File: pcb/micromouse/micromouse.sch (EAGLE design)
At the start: 66 parts, among them IC1 LM2575-5.0WU-(TR), IC2 LM2575-3.3WU-(TR), IC3 DSPIC33FJ64MC804-PT, IC4 L293D, Y1 7.3728MHz

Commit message: Change comment next to series resistors of LEDs (voltage was wrong)
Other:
- note added: "10mA @ 1.2 V"
- note removed: "10mA @ 1.21 V"
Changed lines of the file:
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@@
 max. output current of uC = 15mA.</text>
 <text x="264.16" y="251.46" size="1.778" layer="91">10mA @ 2.1 V</text>
-<text x="264.16" y="261.62" size="1.778" layer="91">10mA @ 1.21 V</text>
+<text x="264.16" y="261.62" size="1.778" layer="91">10mA @ 1.2 V</text>
 <text x="304.8" y="154.94" size="1.778" layer="91">Use socket instead of soldering the
 chip directly onto the board.</text>

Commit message: Fixed ground plate isolation distance, mounting holes and errors
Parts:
- PAD1: value (none) -> TEST_GND
- PAD10: value (none) -> TEST_AVDD
- PAD11: value (none) -> TEST_AVSS
- PAD2: value (none) -> TEST_9V
- PAD3: value (none) -> TEST_5V
- PAD4: value (none) -> TEST_3V3
- PAD5: value (none) -> TEST_PWM1L2
- PAD6: value (none) -> TEST_PWM1L1
- PAD7: value (none) -> TEST_IR0
- PAD8: value (none) -> TEST_IR1
- PAD9: value (none) -> TEST_IR2
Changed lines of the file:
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@@
 <part name="L1" library="Eagle_WE-TIS (rev22a)" deviceset="WE-TIS_1111" device="" package3d_urn="urn:adsk.eagle:package:12988462/4" technology="_7447471331" value="330uH"/>
 <part name="L2" library="Eagle_WE-TIS (rev22a)" deviceset="WE-TIS_1111" device="" package3d_urn="urn:adsk.eagle:package:12988462/4" technology="_7447471331" value="330uH"/>
-<part name="PAD2" library="wirepad" library_urn="urn:adsk.eagle:library:412" deviceset="3,17/1,3" device="" package3d_urn="urn:adsk.eagle:package:30833/1"/>
-<part name="PAD3" library="wirepad" library_urn="urn:adsk.eagle:library:412" deviceset="3,17/1,3" device="" package3d_urn="urn:adsk.eagle:package:30833/1"/>
-<part name="PAD4" library="wirepad" library_urn="urn:adsk.eagle:library:412" deviceset="3,17/1,3" device="" package3d_urn="urn:adsk.eagle:package:30833/1"/>
-<part name="PAD7" library="wirepad" library_urn="urn:adsk.eagle:library:412" deviceset="3,17/1,3" device="" package3d_urn="urn:adsk.eagle:package:30833/1"/>
-<part name="PAD8" library="wirepad" library_urn="urn:adsk.eagle:library:412" deviceset="3,17/1,3" device="" package3d_urn="urn:adsk.eagle:package:30833/1"/>
-<part name="PAD9" library="wirepad" library_urn="urn:adsk.eagle:library:412" deviceset="3,17/1,3" device="" package3d_urn="urn:adsk.eagle:package:30833/1"/>
-<part name="PAD10" library="wirepad" library_urn="urn:adsk.eagle:library:412" deviceset="3,17/1,3" device="" package3d_urn="urn:adsk.eagle:package:30833/1"/>
-<part name="PAD5" library="wirepad" library_urn="urn:adsk.eagle:library:412" deviceset="3,17/1,3" device="" package3d_urn="urn:adsk.eagle:package:30833/1"/>
-<part name="PAD6" library="wirepad" library_urn="urn:adsk.eagle:library:412" deviceset="3,17/1,3" device="" package3d_urn="urn:adsk.eagle:package:30833/1"/>
-<part name="PAD1" library="wirepad" library_urn="urn:adsk.eagle:library:412" deviceset="3,17/1,3" device="" package3d_urn="urn:adsk.eagle:package:30833/1"/>
-<part name="PAD11" library="wirepad" library_urn="urn:adsk.eagle:library:412" deviceset="3,17/1,3" device="" package3d_urn="urn:adsk.eagle:package:30833/1"/>
+<part name="PAD2" library="wirepad" library_urn="urn:adsk.eagle:library:412" deviceset="3,17/1,3" device="" package3d_urn="urn:adsk.eagle:package:30833/1" value="TEST_9V"/>
+<part name="PAD3" library="wirepad" library_urn="urn:adsk.eagle:library:412" deviceset="3,17/1,3" device="" package3d_urn="urn:adsk.eagle:package:30833/1" value="TEST_5V"/>
+<part name="PAD4" library="wirepad" library_urn="urn:adsk.eagle:library:412" deviceset="3,17/1,3" device="" package3d_urn="urn:adsk.eagle:package:30833/1" value="TEST_3V3"/>
+<part name="PAD7" library="wirepad" library_urn="urn:adsk.eagle:library:412" deviceset="3,17/1,3" device="" package3d_urn="urn:adsk.eagle:package:30833/1" value="TEST_IR0"/>
+<part name="PAD8" library="wirepad" library_urn="urn:adsk.eagle:library:412" deviceset="3,17/1,3" device="" package3d_urn="urn:adsk.eagle:package:30833/1" value="TEST_IR1"/>
+<part name="PAD9" library="wirepad" library_urn="urn:adsk.eagle:library:412" deviceset="3,17/1,3" device="" package3d_urn="urn:adsk.eagle:package:30833/1" value="TEST_IR2"/>
+<part name="PAD10" library="wirepad" library_urn="urn:adsk.eagle:library:412" deviceset="3,17/1,3" device="" package3d_urn="urn:adsk.eagle:package:30833/1" value="TEST_AVDD"/>
+<part name="PAD5" library="wirepad" library_urn="urn:adsk.eagle:library:412" deviceset="3,17/1,3" device="" package3d_urn="urn:adsk.eagle:package:30833/1" value="TEST_PWM1L2"/>
+<part name="PAD6" library="wirepad" library_urn="urn:adsk.eagle:library:412" deviceset="3,17/1,3" device="" package3d_urn="urn:adsk.eagle:package:30833/1" value="TEST_PWM1L1"/>
+<part name="PAD1" library="wirepad" library_urn="urn:adsk.eagle:library:412" deviceset="3,17/1,3" device="" package3d_urn="urn:adsk.eagle:package:30833/1" value="TEST_GND"/>
+<part name="PAD11" library="wirepad" library_urn="urn:adsk.eagle:library:412" deviceset="3,17/1,3" device="" package3d_urn="urn:adsk.eagle:package:30833/1" value="TEST_AVSS"/>
 <part name="C5" library="Eagle_WCAP-ATG5 (rev21a)" deviceset="WCAP-ATG5_6.3X11" device="" package3d_urn="urn:adsk.eagle:package:18308010/2" technology="_860020273010" value="330  uF "/>
 <part name="C6" library="Eagle_WCAP-ATG5 (rev21a)" deviceset="WCAP-ATG5_6.3X11" device="" package3d_urn="urn:adsk.eagle:package:18308010/2" technology="_860020273010" value="330  uF "/>
@@
 <instance part="PAD2" gate="1" x="-73.66" y="342.9" smashed="yes" rot="R90">
 <attribute name="NAME" x="-72.9742" y="334.137" size="1.778" layer="95" rot="R90"/>
-<attribute name="VALUE" x="-70.358" y="341.757" size="1.778" layer="96" rot="R90"/>
+<attribute name="VALUE" x="-70.358" y="334.137" size="1.778" layer="96" rot="R90"/>
 </instance>
 <instance part="PAD3" gate="1" x="27.94" y="342.9" smashed="yes" rot="R180">
 <attribute name="NAME" x="36.703" y="343.5858" size="1.778" layer="95" rot="R180"/>
-<attribute name="VALUE" x="29.083" y="346.202" size="1.778" layer="96" rot="R180"/>
+<attribute name="VALUE" x="36.703" y="341.122" size="1.778" layer="96" rot="R180"/>
 </instance>
 <instance part="PAD4" gate="1" x="27.94" y="292.1" smashed="yes" rot="R180">
 <attribute name="NAME" x="36.703" y="292.7858" size="1.778" layer="95" rot="R180"/>
-<attribute name="VALUE" x="29.083" y="295.402" size="1.778" layer="96" rot="R180"/>
+<attribute name="VALUE" x="36.703" y="290.322" size="1.778" layer="96" rot="R180"/>
 </instance>
 <instance part="PAD7" gate="1" x="147.32" y="309.88" smashed="yes" rot="R180">
 <attribute name="NAME" x="156.083" y="310.5658" size="1.778" layer="95" rot="R180"/>
-<attribute name="VALUE" x="148.463" y="313.182" size="1.778" layer="96" rot="R180"/>
+<attribute name="VALUE" x="161.163" y="308.102" size="1.778" layer="96" rot="R180"/>
 </instance>
 <instance part="PAD8" gate="1" x="147.32" y="292.1" smashed="yes" rot="R180">
 <attribute name="NAME" x="156.083" y="292.7858" size="1.778" layer="95" rot="R180"/>
-<attribute name="VALUE" x="148.463" y="295.402" size="1.778" layer="96" rot="R180"/>
+<attribute name="VALUE" x="161.163" y="290.322" size="1.778" layer="96" rot="R180"/>
 </instance>
 <instance part="PAD9" gate="1" x="147.32" y="274.32" smashed="yes" rot="R180">
 <attribute name="NAME" x="156.083" y="275.0058" size="1.778" layer="95" rot="R180"/>
-<attribute name="VALUE" x="148.463" y="277.622" size="1.778" layer="96" rot="R180"/>
+<attribute name="VALUE" x="161.163" y="272.542" size="1.778" layer="96" rot="R180"/>
 </instance>
 <instance part="PAD10" gate="1" x="154.94" y="66.04" smashed="yes" rot="R180">
 <attribute name="NAME" x="166.243" y="66.7258" size="1.778" layer="95" rot="R180"/>
-<attribute name="VALUE" x="156.083" y="69.342" size="1.778" layer="96" rot="R180"/>
+<attribute name="VALUE" x="166.243" y="64.262" size="1.778" layer="96" rot="R180"/>
 </instance>
 <instance part="PAD5" gate="1" x="58.42" y="134.62" smashed="yes">
 <attribute name="NAME" x="49.657" y="133.9342" size="1.778" layer="95"/>
-<attribute name="VALUE" x="57.277" y="131.318" size="1.778" layer="96"/>
+<attribute name="VALUE" x="42.037" y="131.318" size="1.778" layer="96"/>
 </instance>
 <instance part="PAD6" gate="1" x="58.42" y="124.46" smashed="yes">
 <attribute name="NAME" x="49.657" y="123.7742" size="1.778" layer="95"/>
-<attribute name="VALUE" x="57.277" y="121.158" size="1.778" layer="96"/>
+<attribute name="VALUE" x="42.037" y="121.158" size="1.778" layer="96"/>
 </instance>
 <instance part="PAD1" gate="1" x="-86.36" y="340.36" smashed="yes" rot="R180">
 <attribute name="NAME" x="-77.597" y="341.0458" size="1.778" layer="95" rot="R180"/>
-<attribute name="VALUE" x="-85.217" y="343.662" size="1.778" layer="96" rot="R180"/>
+<attribute name="VALUE" x="-77.597" y="338.582" size="1.778" layer="96" rot="R180"/>
 </instance>
 <instance part="PAD11" gate="1" x="154.94" y="53.34" smashed="yes" rot="R180">
 <attribute name="NAME" x="166.243" y="54.0258" size="1.778" layer="95" rot="R180"/>
-<attribute name="VALUE" x="156.083" y="56.642" size="1.778" layer="96" rot="R180"/>
+<attribute name="VALUE" x="166.243" y="51.562" size="1.778" layer="96" rot="R180"/>
 </instance>
 <instance part="C5" gate="G$1" x="25.4" y="325.12" smashed="yes" rot="R90">

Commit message: Almost final steps of PCB, before moving the oscillator
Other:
- note added: "+"
- note added: "Tantulum"
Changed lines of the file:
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@@
 depending on switch position.</text>
 <text x="-58.42" y="223.52" size="1.778" layer="91">Remove some IO if unable to draw all PCB lines</text>
+<text x="8.89" y="115.062" size="1.778" layer="91">+</text>
+<text x="9.144" y="109.982" size="1.778" layer="91">Tantulum</text>
 </plain>
 <instances>

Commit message: Add group name, move via next to oscillator and replace LEDs with low current LEDs.
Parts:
- R5, R7, R9: value 120R -> 680R
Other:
- note added: "2mA * 680R = 1.36V"
- note added: "2mA, 1.9V"
- note removed: "10mA @ 1.2 V"
- note removed: "10mA @ 2.1 V"
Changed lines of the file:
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@@
 <part name="GND11" library="supply1" library_urn="urn:adsk.eagle:library:371" deviceset="GND" device=""/>
 <part name="R1" library="rcl" library_urn="urn:adsk.eagle:library:334" deviceset="R-EU_" device="R0805" package3d_urn="urn:adsk.eagle:package:23553/2" value="10kR"/>
-<part name="R5" library="rcl" library_urn="urn:adsk.eagle:library:334" deviceset="R-EU_" device="R0805" package3d_urn="urn:adsk.eagle:package:23553/2" value="120R"/>
-<part name="R7" library="rcl" library_urn="urn:adsk.eagle:library:334" deviceset="R-EU_" device="R0805" package3d_urn="urn:adsk.eagle:package:23553/2" value="120R"/>
-<part name="R9" library="rcl" library_urn="urn:adsk.eagle:library:334" deviceset="R-EU_" device="R0805" package3d_urn="urn:adsk.eagle:package:23553/2" value="120R"/>
+<part name="R5" library="rcl" library_urn="urn:adsk.eagle:library:334" deviceset="R-EU_" device="R0805" package3d_urn="urn:adsk.eagle:package:23553/2" value="680R"/>
+<part name="R7" library="rcl" library_urn="urn:adsk.eagle:library:334" deviceset="R-EU_" device="R0805" package3d_urn="urn:adsk.eagle:package:23553/2" value="680R"/>
+<part name="R9" library="rcl" library_urn="urn:adsk.eagle:library:334" deviceset="R-EU_" device="R0805" package3d_urn="urn:adsk.eagle:package:23553/2" value="680R"/>
 <part name="C14" library="rcl" library_urn="urn:adsk.eagle:library:334" deviceset="C-EU" device="C0805" package3d_urn="urn:adsk.eagle:package:23617/2" value="100nF"/>
 <part name="C15" library="rcl" library_urn="urn:adsk.eagle:library:334" deviceset="C-EU" device="C0805" package3d_urn="urn:adsk.eagle:package:23617/2" value="100nF"/>
@@
 <text x="218.44" y="228.6" size="1.778" layer="91">p. 357 datasheet of uC:
 max. output current of uC = 15mA.</text>
-<text x="264.16" y="251.46" size="1.778" layer="91">10mA @ 2.1 V</text>
-<text x="264.16" y="261.62" size="1.778" layer="91">10mA @ 1.2 V</text>
+<text x="264.16" y="251.46" size="1.778" layer="91">2mA, 1.9V</text>
+<text x="264.16" y="261.62" size="1.778" layer="91">2mA * 680R = 1.36V</text>
 <text x="304.8" y="154.94" size="1.778" layer="91">Use socket instead of soldering the
 chip directly onto the board.</text>

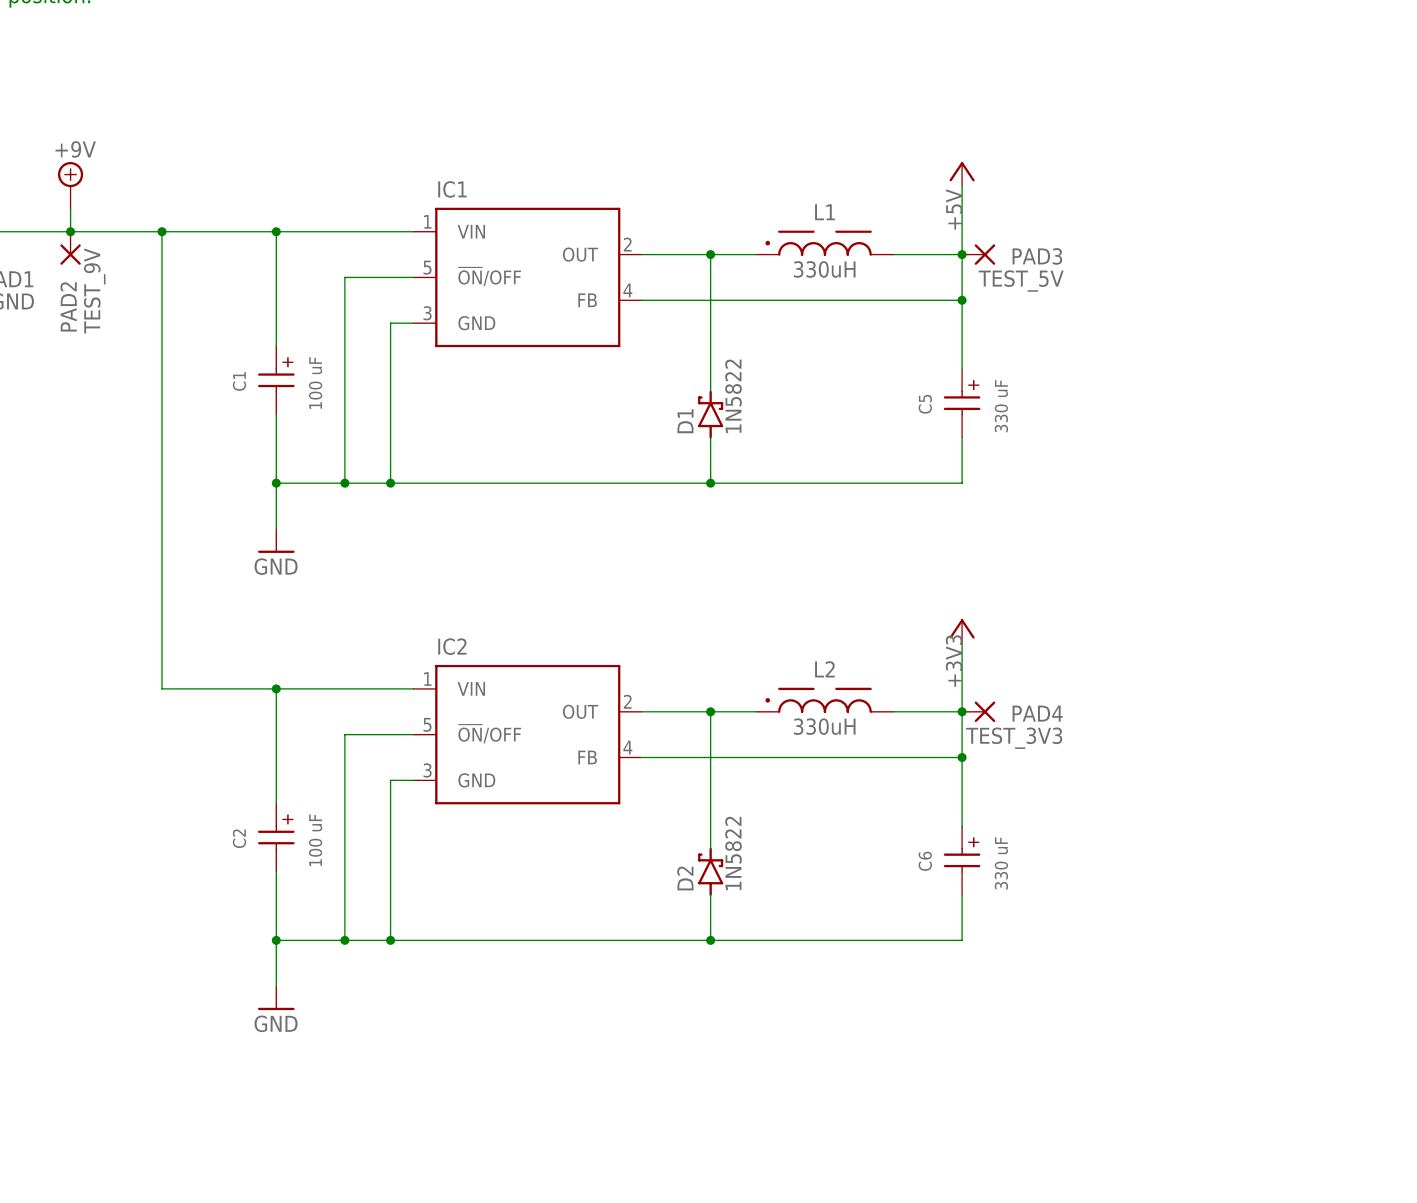
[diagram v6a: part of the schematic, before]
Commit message: Add 100nF capacitors at inputs and outputs of both switching converters. Add vias for ground stitching.
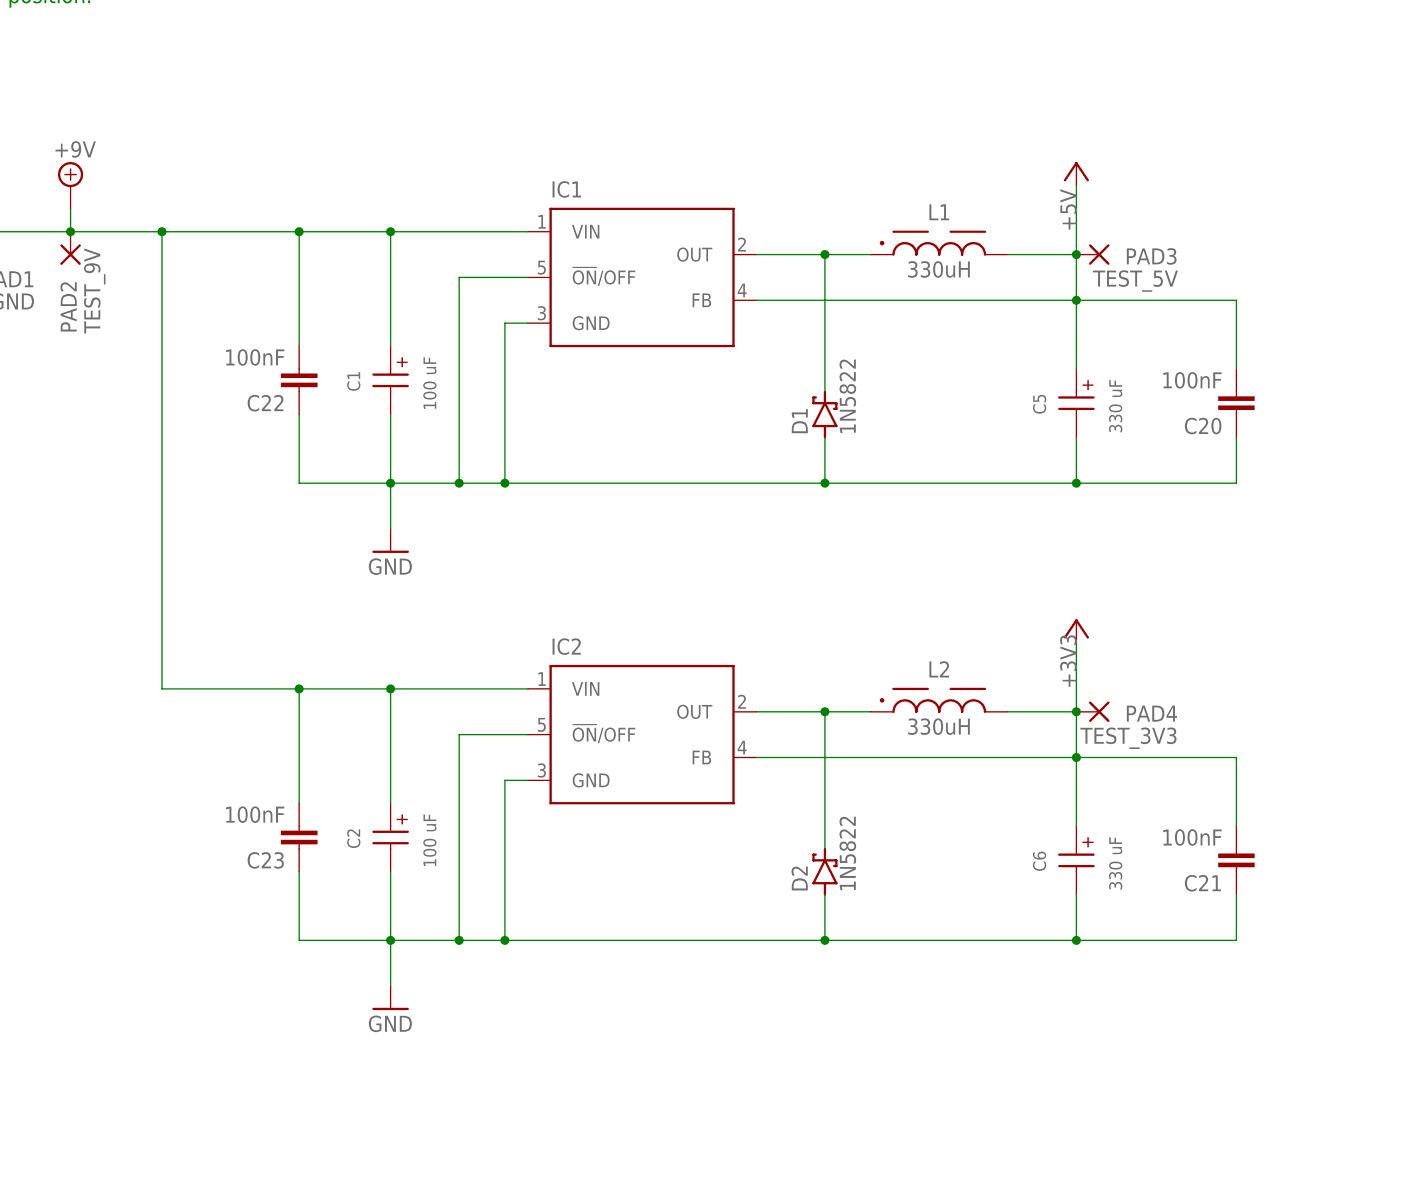
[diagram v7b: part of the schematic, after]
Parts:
- added C20, C21, C22, C23: 100nF, rcl:C-EUC0805
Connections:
- net +3V3: now also C21.2
- net +5V: now also C20.2
- net +9V: now also C22.2, C23.2
- net GND: now also C20.1, C21.1, C22.1, C23.1
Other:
- moved on the sheet: C1, C2, C5, C6, D1, D2, IC1, IC2, L1, L2, PAD3, PAD4
